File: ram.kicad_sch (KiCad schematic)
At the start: 7 parts, among them U1 LFE5U-85F-6BG381C, U2 MT48LC16M16A2TG

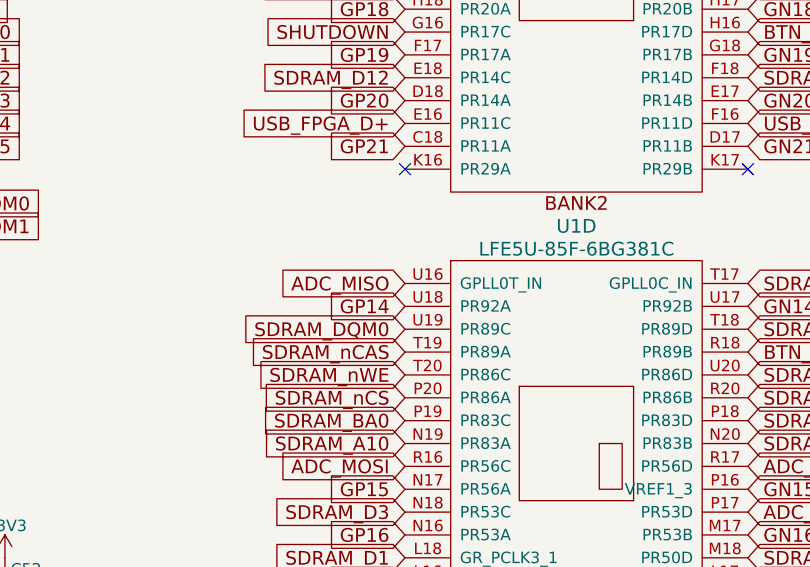
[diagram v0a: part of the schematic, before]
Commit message: remove unneeded components from schema
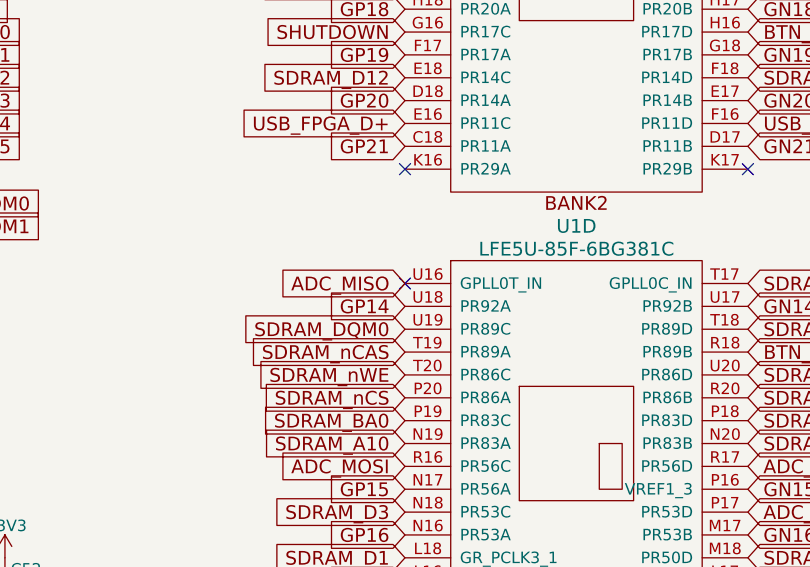
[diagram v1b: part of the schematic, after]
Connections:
- no-connect marks 3 -> 4
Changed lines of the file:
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@@
 		(at 217.17 102.87)
+	)
+	(no_connect
+		(at 217.17 115.57)
 	)
 	(wire

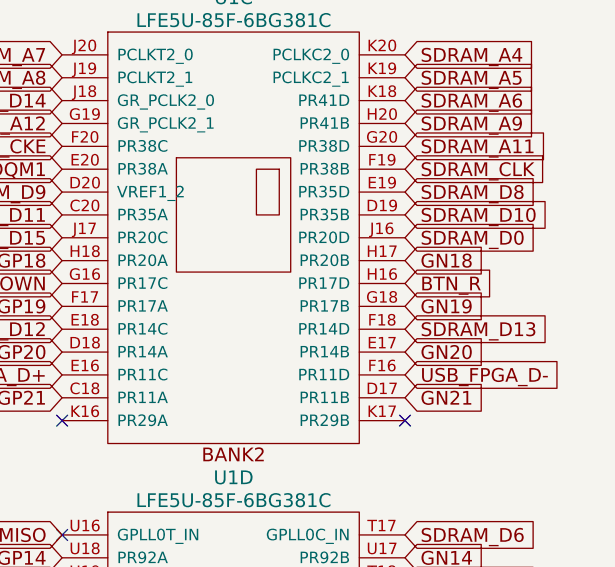
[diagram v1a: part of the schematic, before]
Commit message: remove btn_r, clean trace/via
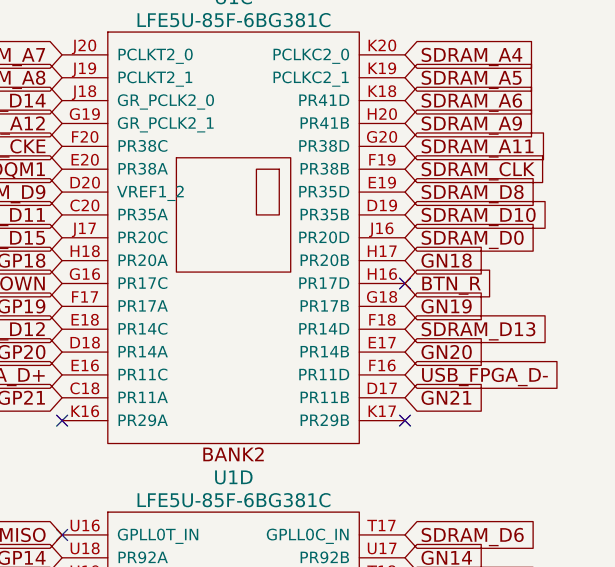
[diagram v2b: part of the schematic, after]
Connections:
- no-connect marks 4 -> 5
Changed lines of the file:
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@@
+	)
+	(no_connect
+		(at 255.27 87.63)
 	)
 	(no_connect

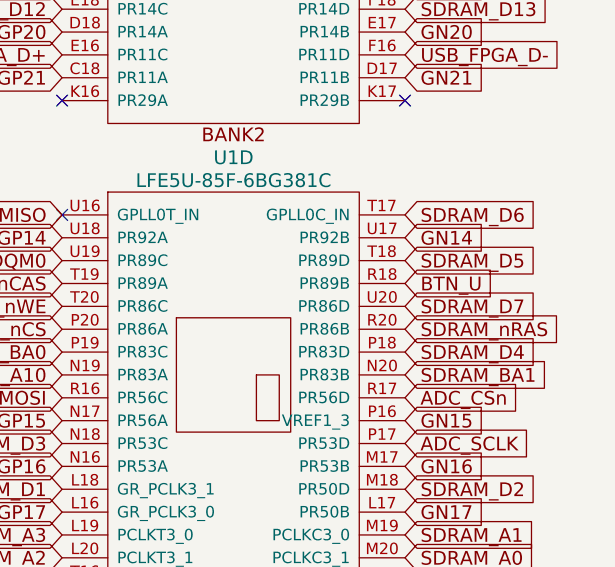
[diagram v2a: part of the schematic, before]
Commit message: mark other button as no-connect, remove tracks
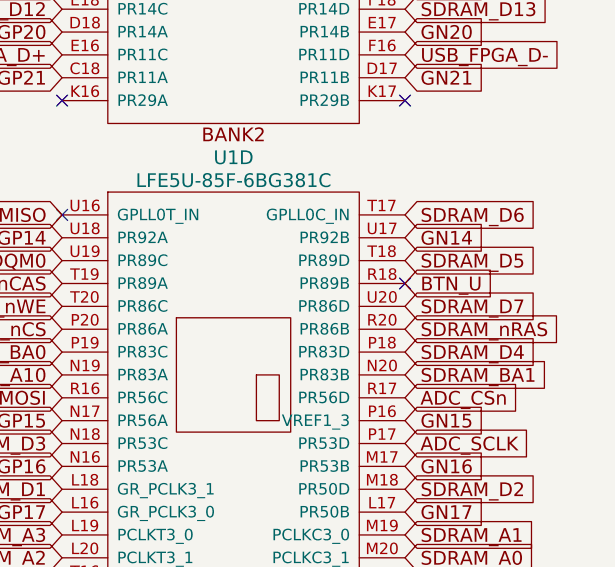
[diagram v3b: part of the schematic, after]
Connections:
- no-connect marks 5 -> 6
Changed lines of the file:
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@@
+	)
+	(no_connect
+		(at 255.27 123.19)
 	)
 	(no_connect

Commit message: start to normalize bom
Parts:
- C16: Digikey (none) -> 587-5918-1-ND; LCSC (none) -> C87995; MPN (none) -> CC0805MRX5R6BB225
- C33, C34, C35, C52: Digikey (none) -> 587-1238-1-ND; LCSC (none) -> C107137
- U1: Digikey (none) -> 220-2177-ND; LCSC (none) -> C446029
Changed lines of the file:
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@@
+			)
+		)
+		(property "LCSC" "C87995"
+			(at 135.89 149.86 0)
+			(effects
+				(font
+					(size 1.27 1.27)
+				)
+				(hide yes)
+			)
+		)
+		(property "Digikey" "587-5918-1-ND"
+			(at 135.89 149.86 0)
+			(effects
+				(font
+					(size 1.27 1.27)
+				)
+				(hide yes)
+			)
+		)
+		(property "MPN" "CC0805MRX5R6BB225"
+			(at 135.89 149.86 0)
+			(effects
+				(font
+					(size 1.27 1.27)
+				)
+				(hide yes)
 			)
 		)
@@
 			)
 		)
+		(property "LCSC" "C446029"
+			(at 236.22 80.01 0)
+			(effects
+				(font
+					(size 1.27 1.27)
+				)
+				(hide yes)
+			)
+		)
+		(property "Digikey" "220-2177-ND"
+			(at 236.22 80.01 0)
+			(effects
+				(font
+					(size 1.27 1.27)
+				)
+				(hide yes)
+			)
+		)
 		(pin "B11"
 		)
@@
 			)
 		)
+		(property "LCSC" "C446029"
+			(at 236.22 133.35 0)
+			(effects
+				(font
+					(size 1.27 1.27)
+				)
+				(hide yes)
+			)
+		)
+		(property "Digikey" "220-2177-ND"
+			(at 236.22 133.35 0)
+			(effects
+				(font
+					(size 1.27 1.27)
+				)
+				(hide yes)
+			)
+		)
 		(pin "B13"
 		)
@@
 			)
 		)
+		(property "LCSC" "C107137"
+			(at 149.86 149.86 0)
+			(effects
+				(font
+					(size 1.27 1.27)
+				)
+				(hide yes)
+			)
+		)
+		(property "Digikey" "587-1238-1-ND"
+			(at 149.86 149.86 0)
+			(effects
+				(font
+					(size 1.27 1.27)
+				)
+				(hide yes)
+			)
+		)
 		(pin "1"
 		)
@@
 			)
 		)
+		(property "LCSC" "C107137"
+			(at 157.48 149.86 0)
+			(effects
+				(font
+					(size 1.27 1.27)
+				)
+				(hide yes)
+			)
+		)
+		(property "Digikey" "587-1238-1-ND"
+			(at 157.48 149.86 0)
+			(effects
+				(font
+					(size 1.27 1.27)
+				)
+				(hide yes)
+			)
+		)
 		(pin "1"
 		)
@@
 			)
 		)
+		(property "LCSC" "C107137"
+			(at 165.1 149.86 0)
+			(effects
+				(font
+					(size 1.27 1.27)
+				)
+				(hide yes)
+			)
+		)
+		(property "Digikey" "587-1238-1-ND"
+			(at 165.1 149.86 0)
+			(effects
+				(font
+					(size 1.27 1.27)
+				)
+				(hide yes)
+			)
+		)
 		(pin "1"
 		)
@@
 			(at 172.72 149.86 0)
 			(effects
+				(font
+					(size 1.27 1.27)
+				)
+				(hide yes)
+			)
+		)
+		(property "LCSC" "C107137"
+			(at 172.72 149.86 0)
+			(effects
+				(font
+					(size 1.27 1.27)
+				)
+				(hide yes)
+			)
+		)
+		(property "Digikey" "587-1238-1-ND"
+			(at 172.72 149.86 0)
+			(effects

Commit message: updating part numbers across schematcs
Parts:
- C33, C34, C35, C52: MPN CX0603MRX7R8BB223 -> CC0603JRX7R8BB223
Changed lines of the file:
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@@
 			)
 		)
-		(property "MPN" "CX0603MRX7R8BB223"
+		(property "MPN" "CC0603JRX7R8BB223"
 			(at 149.86 149.86 0)
 			(effects
@@
 			)
 		)
-		(property "MPN" "CX0603MRX7R8BB223"
+		(property "MPN" "CC0603JRX7R8BB223"
 			(at 157.48 149.86 0)
 			(effects
@@
 			)
 		)
-		(property "MPN" "CX0603MRX7R8BB223"
+		(property "MPN" "CC0603JRX7R8BB223"
 			(at 165.1 149.86 0)
 			(effects
@@
 			)
 		)
-		(property "MPN" "CX0603MRX7R8BB223"
+		(property "MPN" "CC0603JRX7R8BB223"
 			(at 172.72 149.86 0)
 			(effects

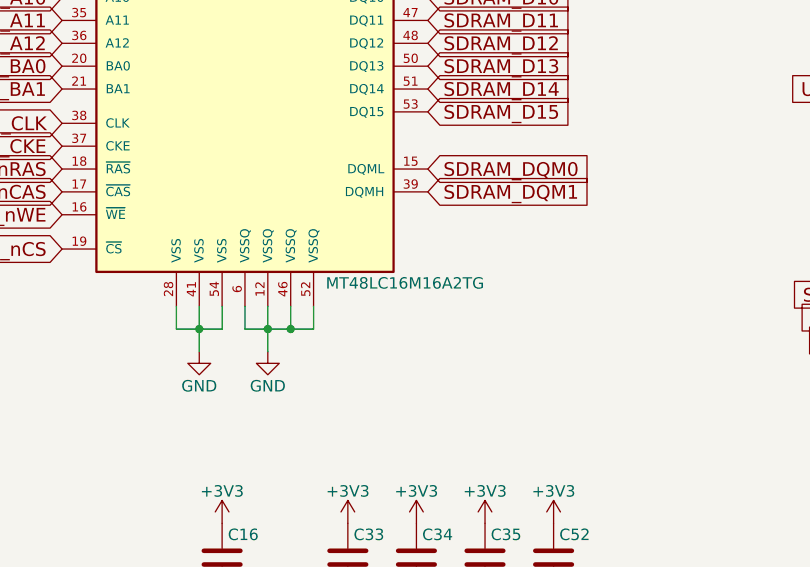
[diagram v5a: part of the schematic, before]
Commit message: migrate ram from MT48LC16M16A2TG-6A to IS42S16160J-6TL
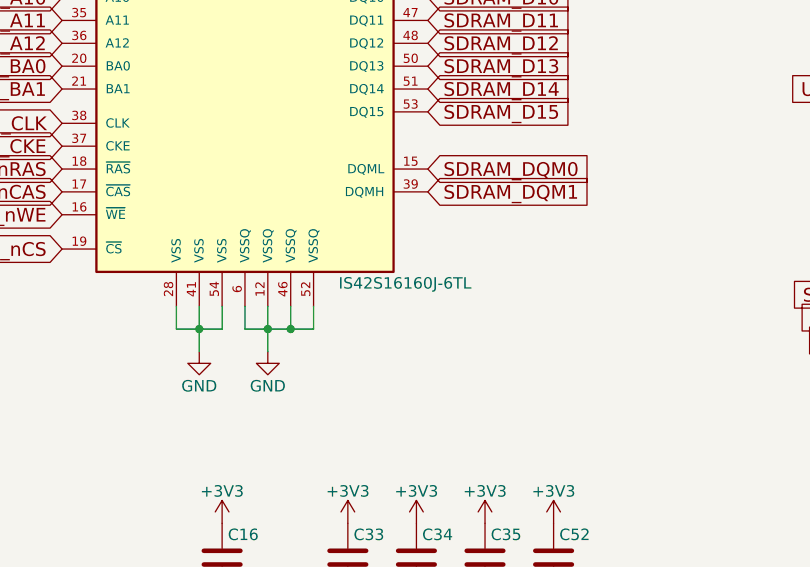
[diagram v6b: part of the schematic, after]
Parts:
- U2: value MT48LC16M16A2TG -> IS42S16160J-6TL; Digikey 1450-1385-1-ND -> (none); LCSC C492195 -> C1353383; LCS_C1 C524867 -> (none); MPN MT48LC16M16A2TG-6A -> 870-IS42S16160J-6TL
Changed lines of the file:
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@@
 			)
 		)
-		(property "Value" "MT48LC16M16A2TG"
+		(property "Value" "IS42S16160J-6TL"
 			(at 156.21 119.38 0)
 			(effects
@@
 			)
 		)
-		(property "MPN" "MT48LC16M16A2TG-6A"
+		(property "MPN" "870-IS42S16160J-6TL"
 			(at 138.43 88.9 0)
 			(effects
@@
 			)
 		)
-		(property "Digikey" "1450-1385-1-ND"
+		(property "Digikey" ""
 			(at 138.43 88.9 0)
 			(effects
@@
 			)
 		)
-		(property "LCSC" "C492195"
-			(at 138.43 88.9 0)
-			(effects
-				(font
-					(size 1.27 1.27)
-				)
-				(hide yes)
-			)
-		)
-		(property "LCS_C1" "C524867"
-			(at 138.43 88.9 0)
-			(effects
+		(property "LCSC" "C1353383"
+			(at 138.43 88.9 0)
+			(effects
+				(font
+					(size 1.27 1.27)
+				)
+				(hide yes)
+			)
+		)
+		(property "LCS_C1" ""
+			(at 138.43 88.9 0)
+			(effects
